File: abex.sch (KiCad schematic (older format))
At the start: 4 parts, among them J1 0877159106, J2 0877159106, J3 0877159106, P1 CONN_01X04

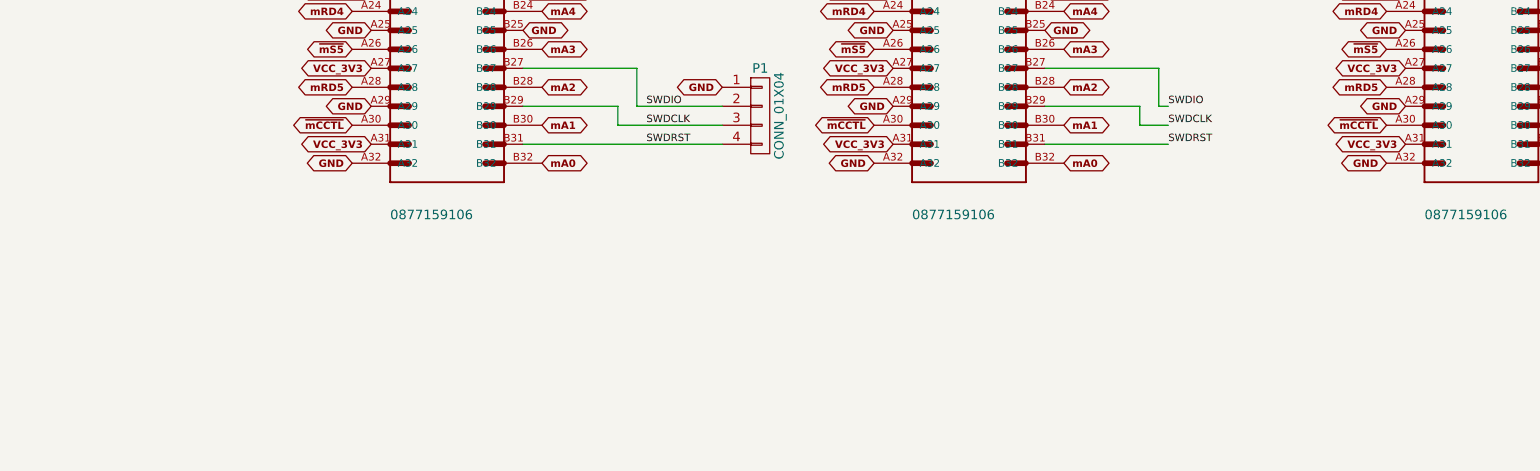
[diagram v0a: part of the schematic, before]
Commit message: Added +5VDC on connector (pin 31). All data & bus signals remain 3.3V tolerant.
Added +5VDC on connector (pin 31). All data & bus signals remain 3.3V
tolerant. If a card need to have 5V signals it need to have all level
shifters needed on board.
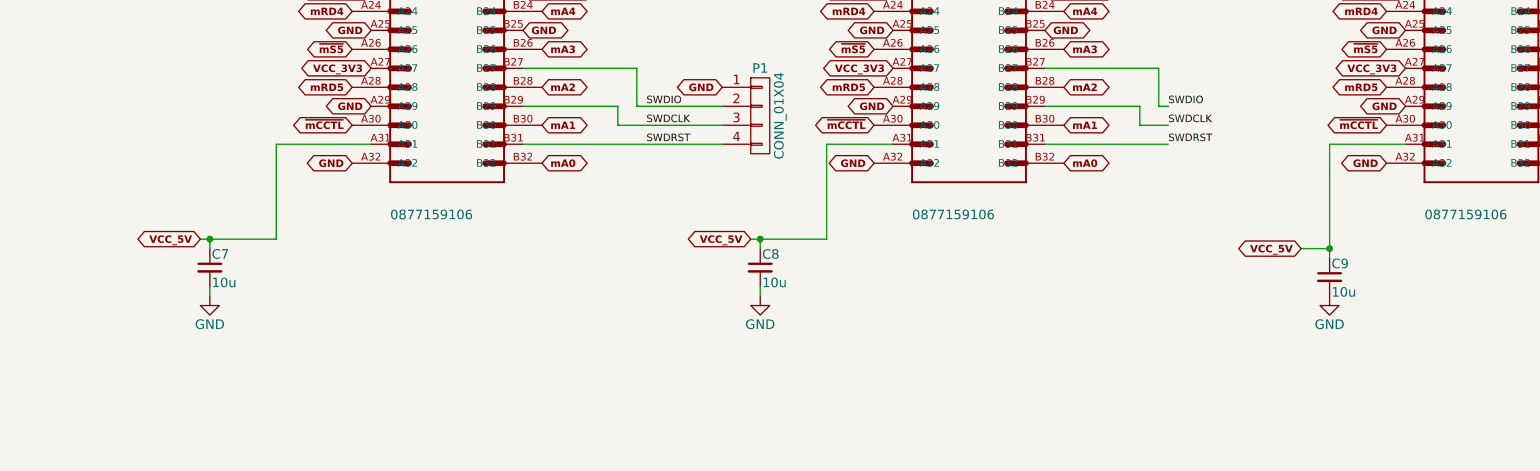
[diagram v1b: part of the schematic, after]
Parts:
- added C7, C8, C9: 10u, Capacitors_SMD:C_1206_HandSoldering, symbol C_Small
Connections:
- net GND: now also C7.2, C8.2, C9.2
- net VCC_3V3: no longer J1.A31, J2.A31, J3.A31
- new net VCC_5V: C7.1, C8.1, C9.1, J1.A31, J2.A31, J3.A31
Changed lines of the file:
@@
 Text GLabel 2850 4500 0    39   BiDi ~ 8
-VCC_3V3
-Text GLabel 2850 4900 0    39   BiDi ~ 8
 VCC_3V3
 Wire Wire Line
@@
 Text GLabel 5600 4500 0    39   BiDi ~ 8
 VCC_3V3
-Text GLabel 5600 4900 0    39   BiDi ~ 8
-VCC_3V3
 Wire Wire Line
 	6400 4700 6900 4700
@@
 Text GLabel 8300 4500 0    39   BiDi ~ 8
 VCC_3V3
-Text GLabel 8300 4900 0    39   BiDi ~ 8
-VCC_3V3
 Wire Wire Line
 	9100 4700 9600 4700
@@
 Wire Wire Line
 	7000 4700 7050 4700
+Text GLabel 7750 5450 0    39   BiDi ~ 8
+VCC_5V
+$Comp
+L GND #PWR01
+U 1 1 5D149D75
+P 7900 5700
+F 0 "#PWR01" H 7900 5450 50  0001 C CNN
+F 1 "GND" H 7900 5550 50  0000 C CNN
+F 2 "" H 7900 5700 50  0001 C CNN
+F 3 "" H 7900 5700 50  0001 C CNN
+	1    7900 5700
+	1    0    0    -1
+$EndComp
+$Comp
+L C_Small C9
+U 1 1 5D149D91
+P 7900 5600
+F 0 "C9" H 7910 5670 50  0000 L CNN
+F 1 "10u" H 7910 5520 50  0000 L CNN
+F 2 "Capacitors_SMD:C_1206_HandSoldering" H 7900 5600 50  0001 C CNN
+F 3 "" H 7900 5600 50  0000 C CNN
+	1    7900 5600
+	1    0    0    -1
+$EndComp
+Text GLabel 4850 5400 0    39   BiDi ~ 8
+VCC_5V
+$Comp
+L GND #PWR02
+U 1 1 5D149F2C
+P 4900 5700
+F 0 "#PWR02" H 4900 5450 50  0001 C CNN
+F 1 "GND" H 4900 5550 50  0000 C CNN
+F 2 "" H 4900 5700 50  0001 C CNN
+F 3 "" H 4900 5700 50  0001 C CNN
+	1    4900 5700
+	1    0    0    -1
+$EndComp
+$Comp
+L C_Small C8
+U 1 1 5D149F32
+P 4900 5550
+F 0 "C8" H 4910 5620 50  0000 L CNN
+F 1 "10u" H 4910 5470 50  0000 L CNN
+F 2 "Capacitors_SMD:C_1206_HandSoldering" H 4900 5550 50  0001 C CNN
+F 3 "" H 4900 5550 50  0000 C CNN
+	1    4900 5550
+	1    0    0    -1
+$EndComp
+Wire Wire Line
+	4900 5400 4900 5450
+Wire Wire Line
+	4900 5650 4900 5700
+Connection ~ 4900 5400
+Wire Wire Line
+	5600 4900 5250 4900
+Wire Wire Line
+	5250 4900 5250 5400
+Wire Wire Line
+	5250 5400 4850 5400
+Text GLabel 1950 5400 0    39   BiDi ~ 8
+VCC_5V
+$Comp
+L GND #PWR03
+U 1 1 5D14A0DB
+P 2000 5700
+F 0 "#PWR03" H 2000 5450 50  0001 C CNN
+F 1 "GND" H 2000 5550 50  0000 C CNN
+F 2 "" H 2000 5700 50  0001 C CNN
+F 3 "" H 2000 5700 50  0001 C CNN
+	1    2000 5700
+	1    0    0    -1
+$EndComp
+$Comp
+L C_Small C7
+U 1 1 5D14A0E1
+P 2000 5550
+F 0 "C7" H 2010 5620 50  0000 L CNN
+F 1 "10u" H 2010 5470 50  0000 L CNN
+F 2 "Capacitors_SMD:C_1206_HandSoldering" H 2000 5550 50  0001 C CNN
+F 3 "" H 2000 5550 50  0000 C CNN
+	1    2000 5550
+	1    0    0    -1
+$EndComp
+Wire Wire Line
+	2000 5400 2000 5450
+Wire Wire Line
+	2000 5650 2000 5700
+Connection ~ 2000 5400
+Wire Wire Line
+	2350 4900 2350 5400
+Wire Wire Line
+	2350 5400 1950 5400
+Wire Wire Line
+	2350 4900 2850 4900
+Wire Wire Line
+	8300 4900 7900 4900
+Wire Wire Line
+	7900 4900 7900 5500
+Wire Wire Line
+	7750 5450 7900 5450
+Connection ~ 7900 5450
 $EndSCHEMATC
